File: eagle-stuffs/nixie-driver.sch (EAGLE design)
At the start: 65 parts, among them IC1 74141N/K155ID1, IC2 74LS595N, IC3 TPS562209, IC4 NE555, Q1 MPSA92, Q10 2N2222, Q11 IRF840, Q12 2N2222, Q2 MPSA92, Q3 MPSA92, Q4 MPSA92, Q5 MPSA42, Q6 MPSA42, Q7 MPSA42, Q8 MPSA42, Q9 PN2907

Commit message: Updated to rev. b
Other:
- note added: "B"
- note removed: "A"
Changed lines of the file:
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@@
 <grid distance="0.1" unitdist="inch" unit="inch" style="lines" multiple="1" display="no" altdistance="0.01" altunitdist="inch" altunit="inch"/>
 <layers>
-<layer number="1" name="Top" color="4" fill="1" visible="yes" active="no"/>
-<layer number="16" name="Bottom" color="1" fill="1" visible="yes" active="no"/>
-<layer number="17" name="Pads" color="2" fill="1" visible="yes" active="no"/>
-<layer number="18" name="Vias" color="2" fill="1" visible="yes" active="no"/>
-<layer number="19" name="Unrouted" color="12" fill="1" visible="yes" active="no"/>
-<layer number="20" name="Dimension" color="15" fill="1" visible="yes" active="no"/>
-<layer number="21" name="tPlace" color="7" fill="1" visible="yes" active="no"/>
-<layer number="22" name="bPlace" color="14" fill="1" visible="yes" active="no"/>
-<layer number="23" name="tOrigins" color="15" fill="1" visible="yes" active="no"/>
-<layer number="24" name="bOrigins" color="15" fill="1" visible="yes" active="no"/>
-<layer number="25" name="tNames" color="7" fill="1" visible="yes" active="no"/>
-<layer number="26" name="bNames" color="7" fill="1" visible="yes" active="no"/>
-<layer number="27" name="tValues" color="7" fill="1" visible="yes" active="no"/>
-<layer number="28" name="bValues" color="7" fill="1" visible="yes" active="no"/>
+<layer number="1" name="Top" color="4" fill="1" visible="no" active="no"/>
+<layer number="16" name="Bottom" color="1" fill="1" visible="no" active="no"/>
+<layer number="17" name="Pads" color="2" fill="1" visible="no" active="no"/>
+<layer number="18" name="Vias" color="2" fill="1" visible="no" active="no"/>
+<layer number="19" name="Unrouted" color="12" fill="1" visible="no" active="no"/>
+<layer number="20" name="Dimension" color="15" fill="1" visible="no" active="no"/>
+<layer number="21" name="tPlace" color="7" fill="1" visible="no" active="no"/>
+<layer number="22" name="bPlace" color="14" fill="1" visible="no" active="no"/>
+<layer number="23" name="tOrigins" color="15" fill="1" visible="no" active="no"/>
+<layer number="24" name="bOrigins" color="15" fill="1" visible="no" active="no"/>
+<layer number="25" name="tNames" color="7" fill="1" visible="no" active="no"/>
+<layer number="26" name="bNames" color="7" fill="1" visible="no" active="no"/>
+<layer number="27" name="tValues" color="7" fill="1" visible="no" active="no"/>
+<layer number="28" name="bValues" color="7" fill="1" visible="no" active="no"/>
 <layer number="29" name="tStop" color="7" fill="3" visible="no" active="no"/>
 <layer number="30" name="bStop" color="7" fill="6" visible="no" active="no"/>
@@
 <layer number="35" name="tGlue" color="7" fill="4" visible="no" active="no"/>
 <layer number="36" name="bGlue" color="7" fill="5" visible="no" active="no"/>
-<layer number="37" name="tTest" color="7" fill="1" visible="yes" active="no"/>
-<layer number="38" name="bTest" color="7" fill="1" visible="yes" active="no"/>
+<layer number="37" name="tTest" color="7" fill="1" visible="no" active="no"/>
+<layer number="38" name="bTest" color="7" fill="1" visible="no" active="no"/>
 <layer number="39" name="tKeepout" color="4" fill="11" visible="no" active="no"/>
 <layer number="40" name="bKeepout" color="1" fill="11" visible="no" active="no"/>
@@
 <layer number="44" name="Drills" color="7" fill="1" visible="no" active="no"/>
 <layer number="45" name="Holes" color="7" fill="1" visible="no" active="no"/>
-<layer number="46" name="Milling" color="3" fill="1" visible="yes" active="no"/>
-<layer number="47" name="Measures" color="7" fill="1" visible="yes" active="no"/>
-<layer number="48" name="Document" color="7" fill="1" visible="yes" active="no"/>
-<layer number="49" name="Reference" color="7" fill="1" visible="yes" active="no"/>
-<layer number="51" name="tDocu" color="6" fill="1" visible="yes" active="no"/>
-<layer number="52" name="bDocu" color="7" fill="1" visible="yes" active="no"/>
+<layer number="46" name="Milling" color="3" fill="1" visible="no" active="no"/>
+<layer number="47" name="Measures" color="7" fill="1" visible="no" active="no"/>
+<layer number="48" name="Document" color="7" fill="1" visible="no" active="no"/>
+<layer number="49" name="Reference" color="7" fill="1" visible="no" active="no"/>
+<layer number="51" name="tDocu" color="6" fill="1" visible="no" active="no"/>
+<layer number="52" name="bDocu" color="7" fill="1" visible="no" active="no"/>
 <layer number="90" name="Modules" color="5" fill="1" visible="yes" active="yes"/>
 <layer number="91" name="Nets" color="2" fill="1" visible="yes" active="yes"/>
@@
 <text x="175.26" y="30.48" size="2.54" layer="98" font="fixed">Author:</text>
 <text x="190.5" y="30.48" size="2.54" layer="98" font="fixed">Steve Sirois</text>
-<text x="266.7" y="7.62" size="2.54" layer="98" font="fixed">A</text>
+<text x="266.7" y="7.62" size="2.54" layer="98" font="fixed">B</text>
 <text x="175.26" y="25.4" size="2.54" layer="98" font="fixed">Project:</text>
 <text x="193.04" y="25.4" size="2.54" layer="98" font="fixed">Y.A.N.C. (Yet Another Nixie Clock)</text>

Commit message: Added some info
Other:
- note added: "Power supply output (+5v / 500mA, +170v / 6 mA)"
- note removed: "Power supply (+5v / 500mA, +170v / 6 mA)"
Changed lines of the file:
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@@
 <wire x1="144.78" y1="99.06" x2="7.62" y2="99.06" width="0.1524" layer="98" style="shortdash"/>
 <wire x1="7.62" y1="99.06" x2="7.62" y2="203.2" width="0.1524" layer="98" style="shortdash"/>
-<text x="38.1" y="208.28" size="1.778" layer="98">Power supply (+5v / 500mA, +170v / 6 mA)</text>
+<text x="38.1" y="208.28" size="1.778" layer="98">Power supply output (+5v / 500mA, +170v / 6 mA)</text>
 <text x="223.52" y="45.72" size="1.778" layer="98">Cathode drivers &amp; Ambient led</text>
 <wire x1="147.32" y1="134.62" x2="269.24" y2="134.62" width="0.1524" layer="98" style="shortdash"/>

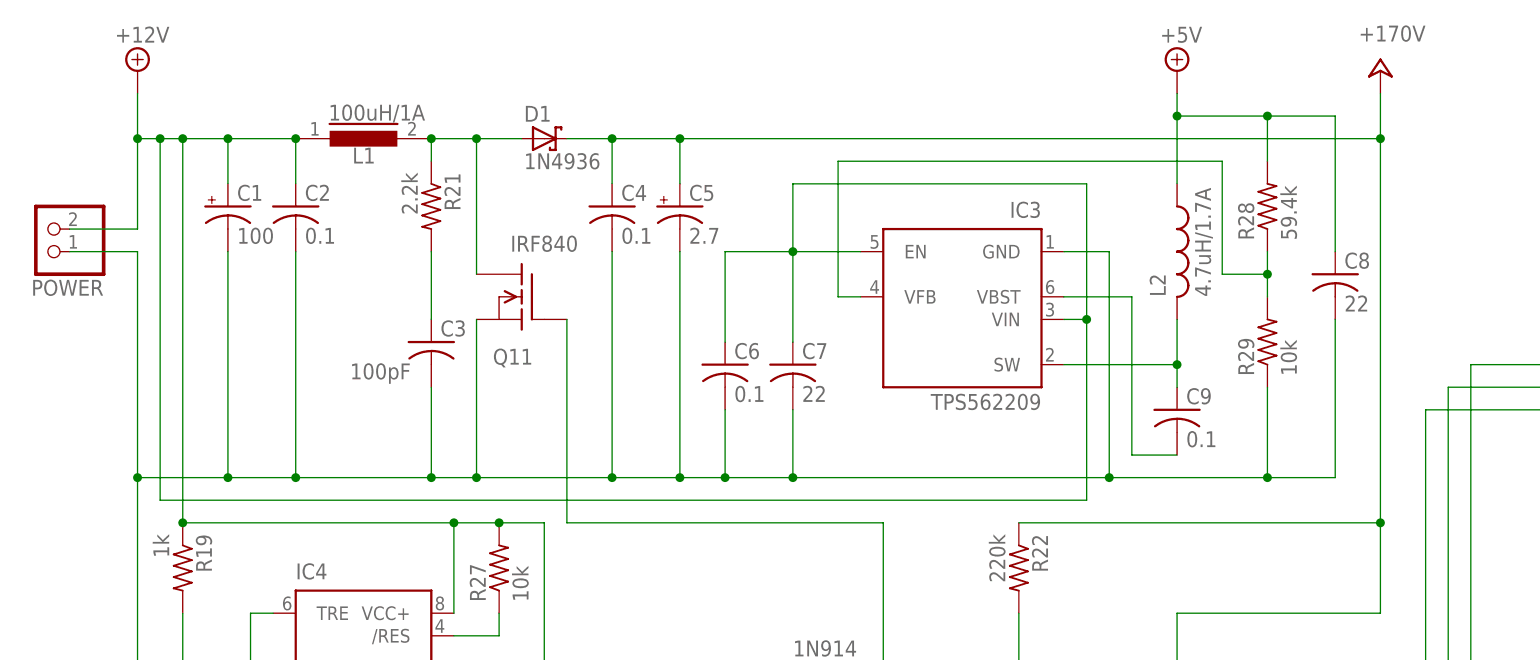
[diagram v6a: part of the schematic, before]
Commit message: Discarded the TPS562209
Too sensitive to touch (touching the chip, blow-it up!
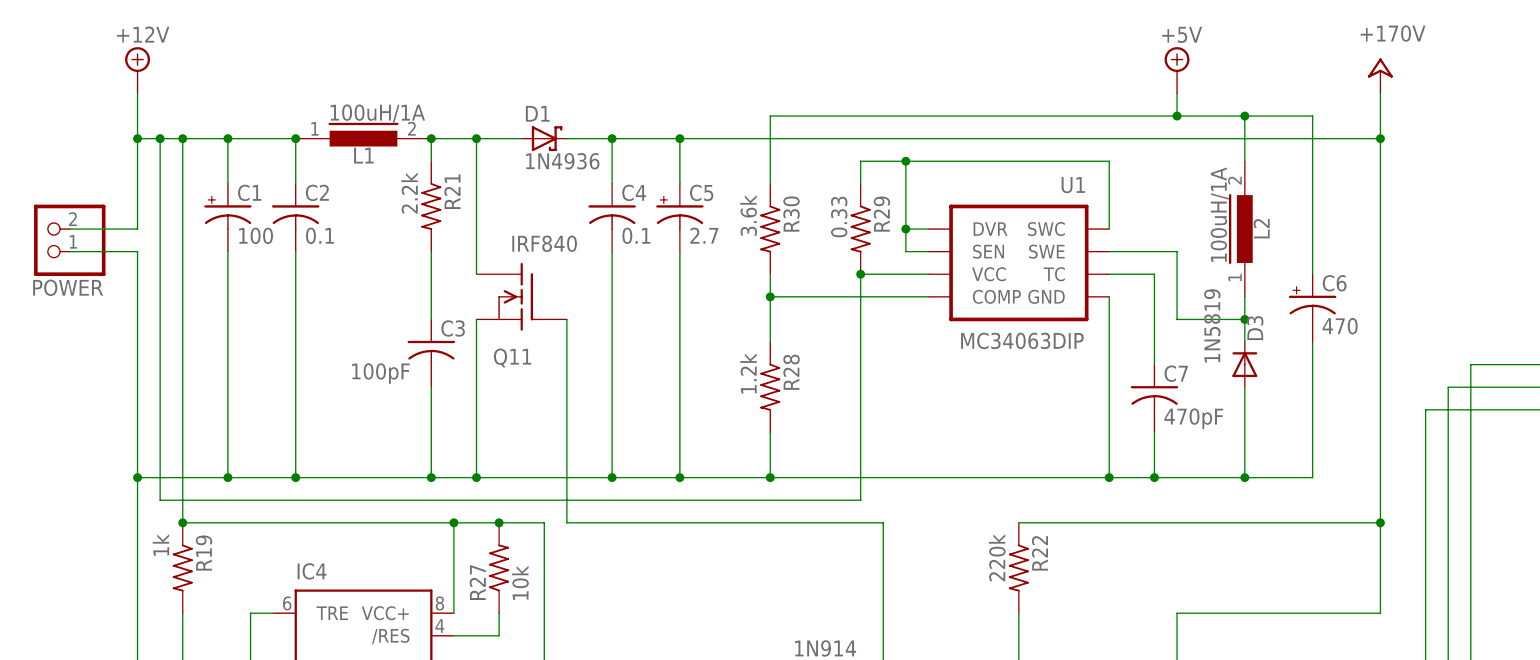
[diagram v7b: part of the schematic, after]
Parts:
- removed C8: 22, rcl:C-US050-024X044
- removed C9: 0.1, rcl:C-US050-024X044
- removed IC3: TPS562209, texas:TPS61070DDC
- added D3: 1N5819, diode:1N4004
- added R30: 3.6k, resistor:R-US_0207/10
- added U1: MC34063DIP, SparkFun-PowerIC:MC34063DIP
- C6: value 0.1 -> 470; device rcl:C-US050-024X044 -> rcl:CPOL-USE3.5-8
- C7: value 22 -> 470pF
- L2: value 4.7uH/1.7A -> 100uH/1A; device resistor:L-US0207/12 -> inductors:MMICC7
- R28: value 59.4k -> 1.2k; device resistor:R-US_0204/2V -> resistor:R-US_0207/10
- R29: value 10k -> 0.33; device resistor:R-US_0204/2V -> resistor:R-US_0207/10
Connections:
- removed net SW: C9.1, IC3.SW, L2.2
- removed net VBST: C9.2, IC3.VBST
- removed net VFB: IC3.VFB, R28.1, R29.2
- new net N$57: R29.1, U1.DVR, U1.SEN, U1.SWC
- new net N$67: R28.1, R30.2, U1.COMP
- new net N$68: C7.1, U1.TC
- new net N$69: D3.C, L2.1, U1.SWE
- net +12V: now also R29.2, U1.VCC; no longer C6.1, C7.1, IC3.EN, IC3.VIN
- net +5V: now also C6.+, L2.2, R30.1; no longer C8.1, L2.1, R28.2
- net GND: now also C6.-, D3.A, R28.2, U1.GND; no longer C6.2, C8.2, IC3.GND, R29.1
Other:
- note added: "C"
- note added: "Power supply output (+5v/700mA, +170v/10mA)"
- note removed: "B"
- note removed: "Power supply output (+5v / 500mA, +170v / 6 mA)"
- moved on the sheet: C7, R28, R29

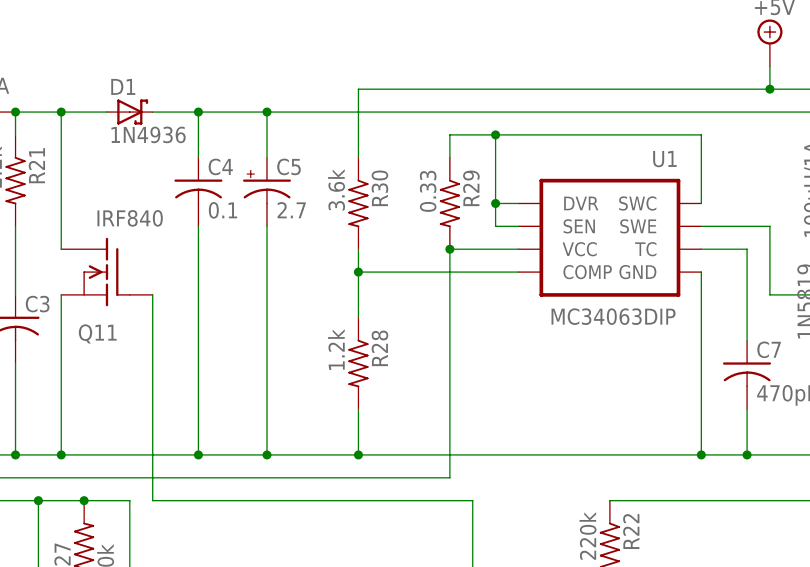
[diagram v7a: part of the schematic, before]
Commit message: Ajusted layout + add backplane shield
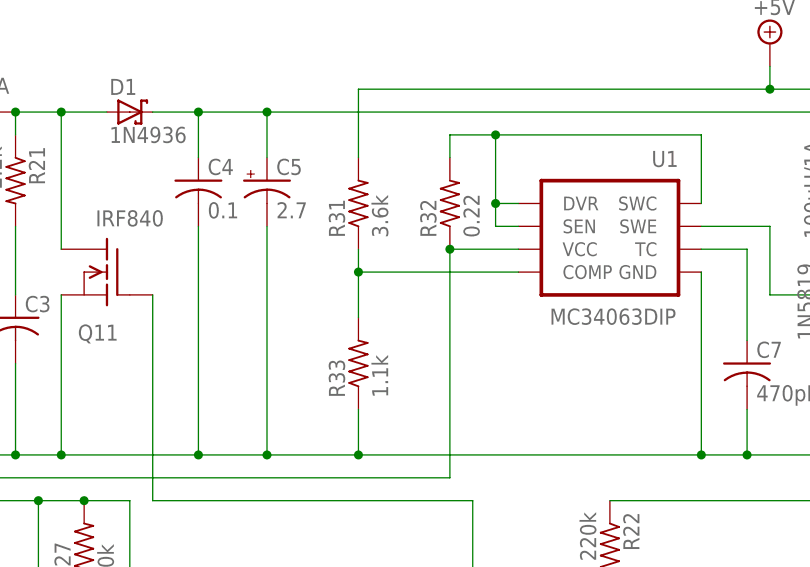
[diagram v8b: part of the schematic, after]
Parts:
- removed R28: 1.2k, resistor:R-US_0207/10
- removed R29: 0.33, resistor:R-US_0207/10
- removed R30: 3.6k, resistor:R-US_0207/10
- added R31: 3.6k, resistor:R-US_0204/2V
- added R32: 0.22, resistor:R-US_0204/2V
- added R33: 1.1k, resistor:R-US_0204/2V
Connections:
- net +12V: now also R32.1; no longer R29.2
- net +5V: now also R31.2; no longer R30.1
- net GND: now also R33.1; no longer R28.2
- net N$57: now also R32.2; no longer R29.1
- net N$67: now also R31.1, R33.2; no longer R28.1, R30.2
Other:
- note added: "Power supply output (+5v/750mA, +170v/10mA)"
- note removed: "Power supply output (+5v/700mA, +170v/10mA)"
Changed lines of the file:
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@@
 <part name="R24" library="pot" deviceset="TRIM_EU-" device="CA6V" value="2k"/>
 <part name="U1" library="SparkFun-PowerIC" deviceset="MC34063" device="DIP"/>
-<part name="R28" library="resistor" deviceset="R-US_" device="0207/10" value="1.2k"/>
-<part name="R29" library="resistor" deviceset="R-US_" device="0207/10" value="0.33"/>
-<part name="R30" library="resistor" deviceset="R-US_" device="0207/10" value="3.6k"/>
 <part name="D3" library="diode" deviceset="1N4004" device="" value="1N5819"/>
 <part name="L2" library="inductors" deviceset="MMICC7" device="" value="100uH/1A"/>
 <part name="C6" library="rcl" deviceset="CPOL-US" device="E3.5-8" value="470"/>
 <part name="C7" library="rcl" deviceset="C-US" device="050-024X044" value="470pF"/>
+<part name="R31" library="resistor" deviceset="R-US_" device="0204/2V" value="3.6k"/>
+<part name="R32" library="resistor" deviceset="R-US_" device="0204/2V" value="0.22"/>
+<part name="R33" library="resistor" deviceset="R-US_" device="0204/2V" value="1.1k"/>
 </parts>
 <sheets>
@@
 <wire x1="144.78" y1="99.06" x2="7.62" y2="99.06" width="0.1524" layer="98" style="shortdash"/>
 <wire x1="7.62" y1="99.06" x2="7.62" y2="203.2" width="0.1524" layer="98" style="shortdash"/>
-<text x="38.1" y="208.28" size="1.778" layer="98">Power supply output (+5v/700mA, +170v/10mA)</text>
+<text x="38.1" y="208.28" size="1.778" layer="98">Power supply output (+5v/750mA, +170v/10mA)</text>
 <text x="223.52" y="45.72" size="1.778" layer="98">Cathode drivers &amp; Ambient led</text>
 <wire x1="147.32" y1="134.62" x2="269.24" y2="134.62" width="0.1524" layer="98" style="shortdash"/>
@@
 <instance part="R24" gate="1" x="121.92" y="129.54" rot="R180"/>
 <instance part="U1" gate="G$1" x="121.92" y="182.88" rot="MR0"/>
-<instance part="R28" gate="G$1" x="93.98" y="170.18" smashed="yes" rot="R270">
-<attribute name="NAME" x="95.4786" y="173.99" size="1.778" layer="95" rot="R270"/>
-<attribute name="VALUE" x="90.678" y="173.99" size="1.778" layer="96" rot="R270"/>
-</instance>
-<instance part="R29" gate="G$1" x="104.14" y="187.96" smashed="yes" rot="R270">
-<attribute name="NAME" x="105.6386" y="191.77" size="1.778" layer="95" rot="R270"/>
-<attribute name="VALUE" x="100.838" y="191.77" size="1.778" layer="96" rot="R270"/>
-</instance>
-<instance part="R30" gate="G$1" x="93.98" y="187.96" smashed="yes" rot="R270">
-<attribute name="NAME" x="95.4786" y="191.77" size="1.778" layer="95" rot="R270"/>
-<attribute name="VALUE" x="90.678" y="191.77" size="1.778" layer="96" rot="R270"/>
-</instance>
 <instance part="D3" gate="1" x="147.32" y="172.72" smashed="yes" rot="R90">
 <attribute name="NAME" x="149.3774" y="175.26" size="1.778" layer="95" rot="R90"/>
@@
 <instance part="C6" gate="G$1" x="154.94" y="180.34"/>
 <instance part="C7" gate="G$1" x="137.16" y="170.18"/>
+<instance part="R31" gate="G$1" x="93.98" y="187.96" rot="R90"/>
+<instance part="R32" gate="G$1" x="104.14" y="187.96" rot="R90"/>
+<instance part="R33" gate="G$1" x="93.98" y="170.18" rot="R90"/>
 </instances>
 <busses>
@@
 <pinref part="C2" gate="G$1" pin="1"/>
 <pinref part="U1" gate="G$1" pin="VCC"/>
-<pinref part="R29" gate="G$1" pin="2"/>
 <wire x1="111.76" y1="182.88" x2="104.14" y2="182.88" width="0.1524" layer="91"/>
 <wire x1="104.14" y1="157.48" x2="104.14" y2="182.88" width="0.1524" layer="91"/>
+<pinref part="R32" gate="G$1" pin="1"/>
 <junction x="104.14" y="182.88"/>
 </segment>
@@
 <pinref part="Q10" gate="G$1" pin="E"/>
 <pinref part="C10" gate="G$1" pin="2"/>
-<pinref part="R28" gate="G$1" pin="2"/>
 <wire x1="93.98" y1="165.1" x2="93.98" y2="160.02" width="0.1524" layer="91"/>
 <junction x="93.98" y="160.02"/>
@@
 <wire x1="154.94" y1="160.02" x2="154.94" y2="175.26" width="0.1524" layer="91"/>
 <junction x="147.32" y="160.02"/>
+<pinref part="R33" gate="G$1" pin="1"/>
 </segment>
 <segment>
@@
 <pinref part="SUPPLY2" gate="+5V" pin="+5V"/>
 <wire x1="139.7" y1="200.66" x2="139.7" y2="203.2" width="0.1524" layer="91"/>
-<pinref part="R30" gate="G$1" pin="1"/>
 <wire x1="139.7" y1="200.66" x2="93.98" y2="200.66" width="0.1524" layer="91"/>
 <wire x1="93.98" y1="200.66" x2="93.98" y2="193.04" width="0.1524" layer="91"/>
@@
 <wire x1="154.94" y1="200.66" x2="154.94" y2="182.88" width="0.1524" layer="91"/>
 <junction x="147.32" y="200.66"/>
+<pinref part="R31" gate="G$1" pin="2"/>
 </segment>
 <segment>
@@
 <wire x1="111.76" y1="187.96" x2="109.22" y2="187.96" width="0.1524" layer="91"/>
 <junction x="109.22" y="187.96"/>
-<pinref part="R29" gate="G$1" pin="1"/>
 <wire x1="109.22" y1="195.58" x2="104.14" y2="195.58" width="0.1524" layer="91"/>
 <wire x1="104.14" y1="195.58" x2="104.14" y2="193.04" width="0.1524" layer="91"/>
 <junction x="109.22" y="195.58"/>
+<pinref part="R32" gate="G$1" pin="2"/>
 </segment>
 </net>
 <net name="N$67" class="0">
 <segment>
-<pinref part="R28" gate="G$1" pin="1"/>
-<pinref part="R30" gate="G$1" pin="2"/>
 <wire x1="93.98" y1="175.26" x2="93.98" y2="180.34" width="0.1524" layer="91"/>
 <pinref part="U1" gate="G$1" pin="COMP"/>
@@
 <wire x1="111.76" y1="180.34" x2="93.98" y2="180.34" width="0.1524" layer="91"/>
 <junction x="93.98" y="180.34"/>
-</segment>
-</net>
+<pinref part="R31" gate="G$1" pin="1"/>
+<pinref part="R33" gate="G$1" pin="2"/>
+</segment>
+</net>
